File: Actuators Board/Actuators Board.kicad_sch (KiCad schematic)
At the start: 68 parts, among them IC1 BD62120AEFJ-E2, J1 Conn_01x05_Male, J10 Conn_01x02_Male, J2 Solenoid(Sol), J4 Conn_01x03_Male, J5 Conn_01x06_Male, J9 Conn_01x02_Male, Q1 MMDT2222A, Q2 SI2366DS, U1 ESP32-PICO-D4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

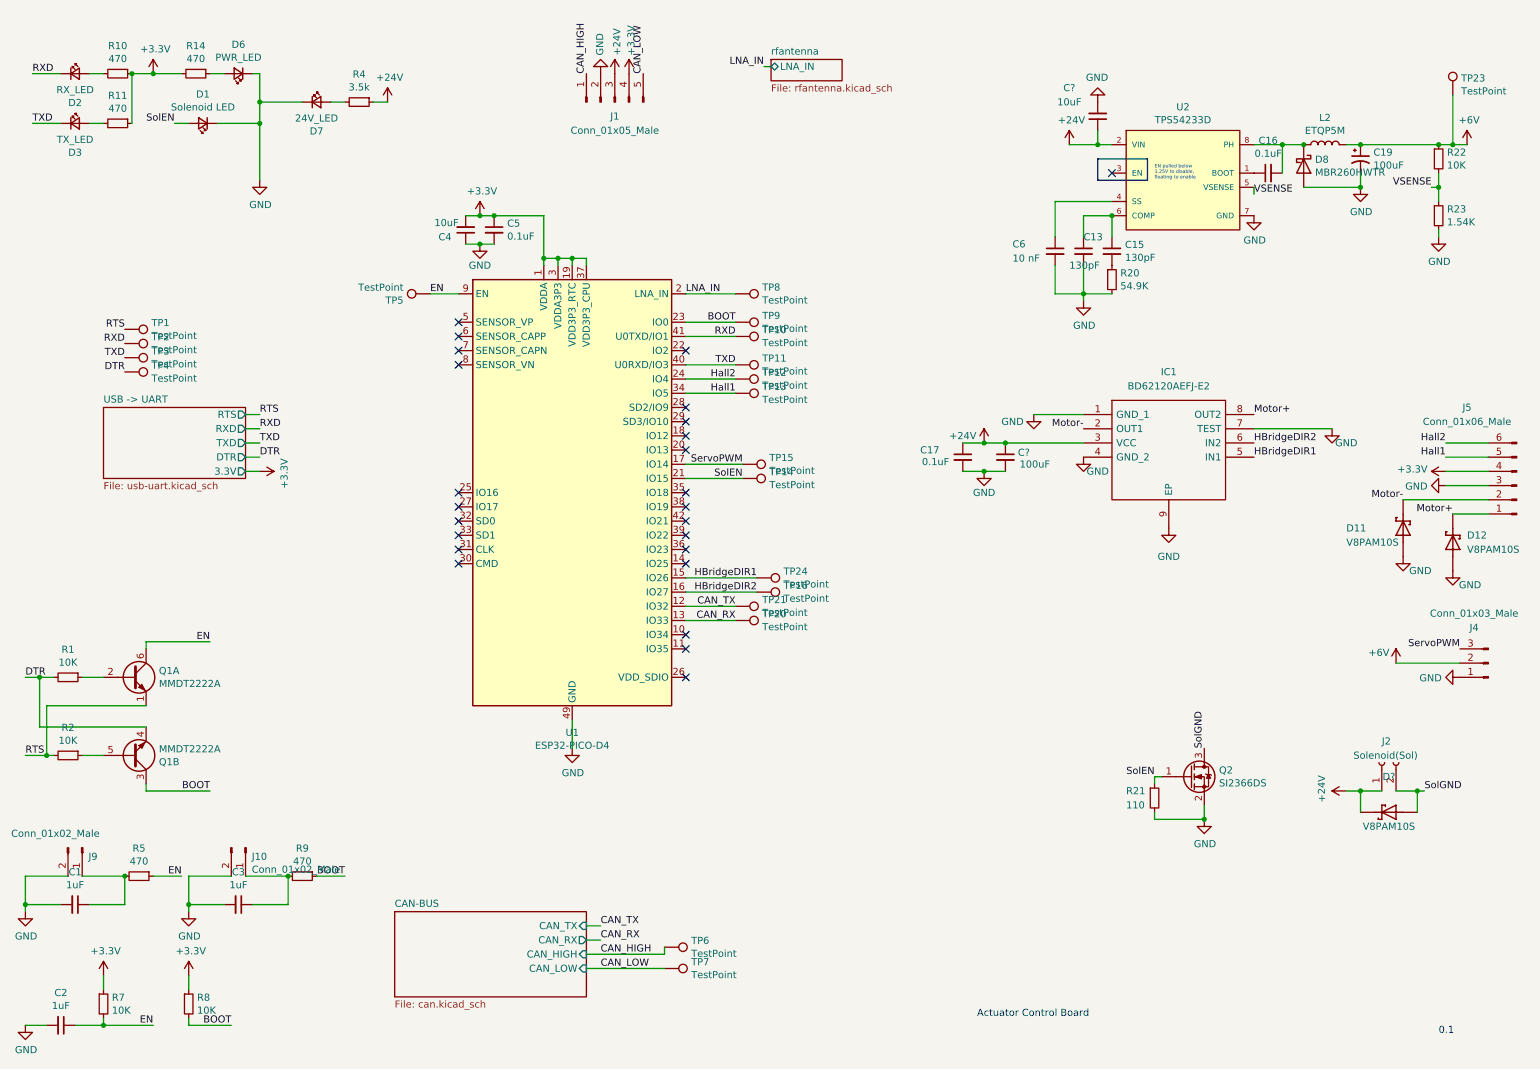
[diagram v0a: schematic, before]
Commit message: Added LDO for 5 -> 3.3V
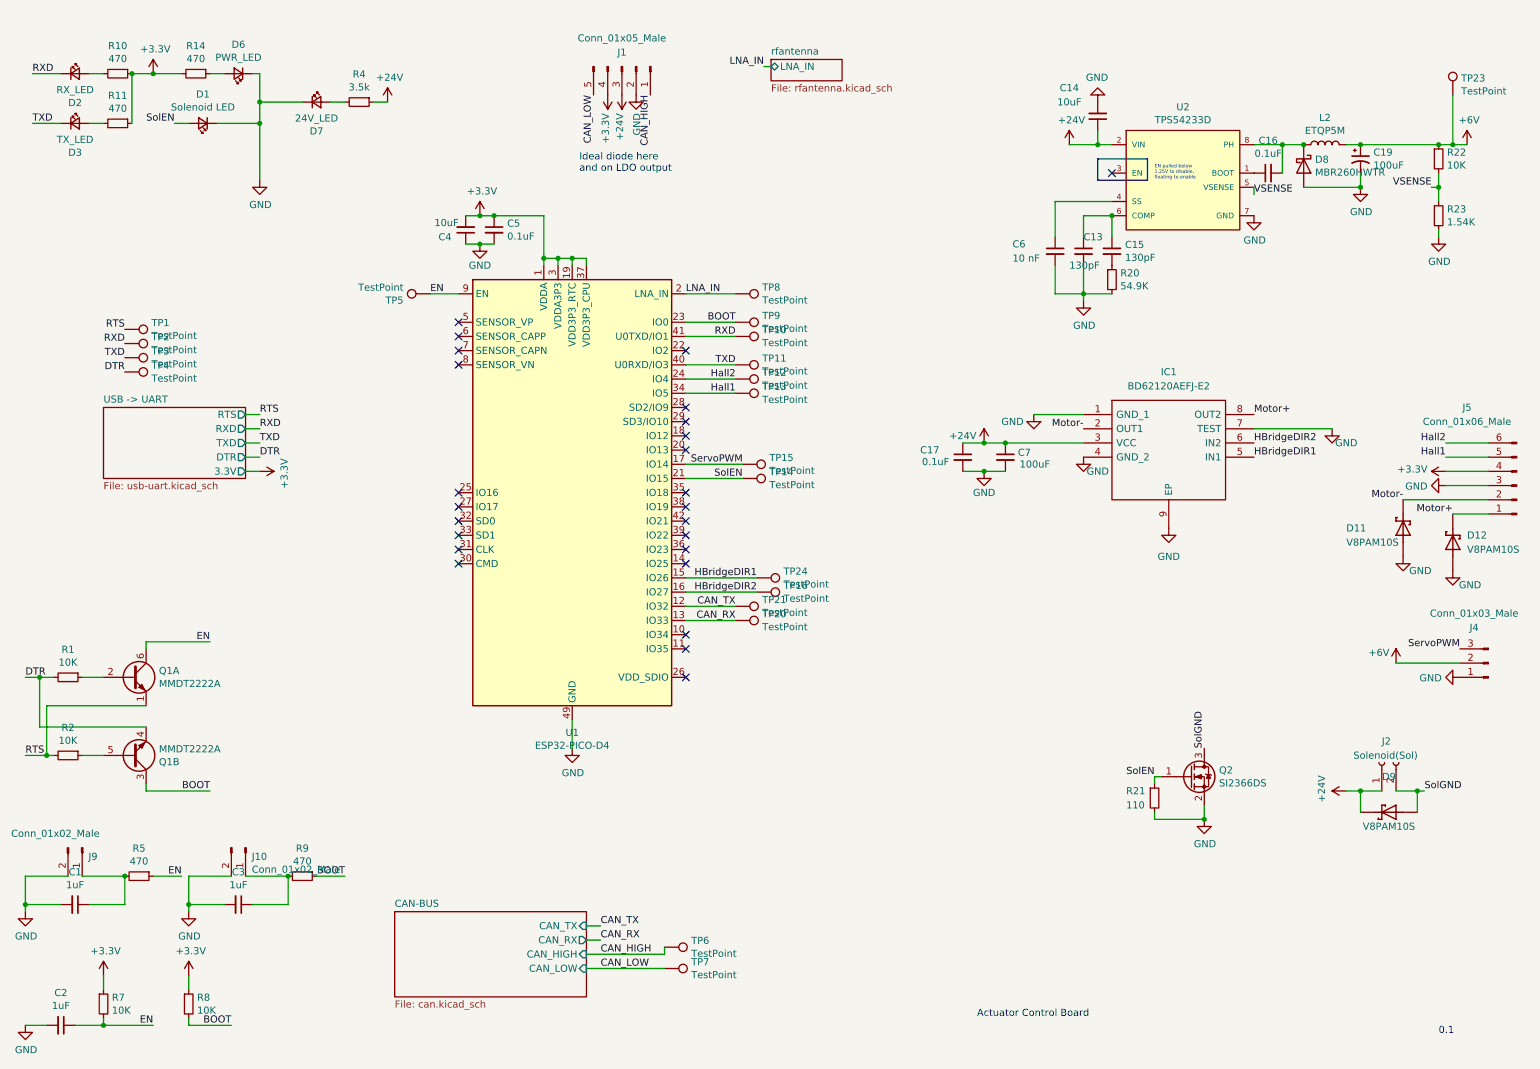
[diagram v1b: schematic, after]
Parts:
- gave numbers to parts that had none: 3
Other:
- note added: "Ideal diode here and on LDO output"
- moved on the sheet: J1

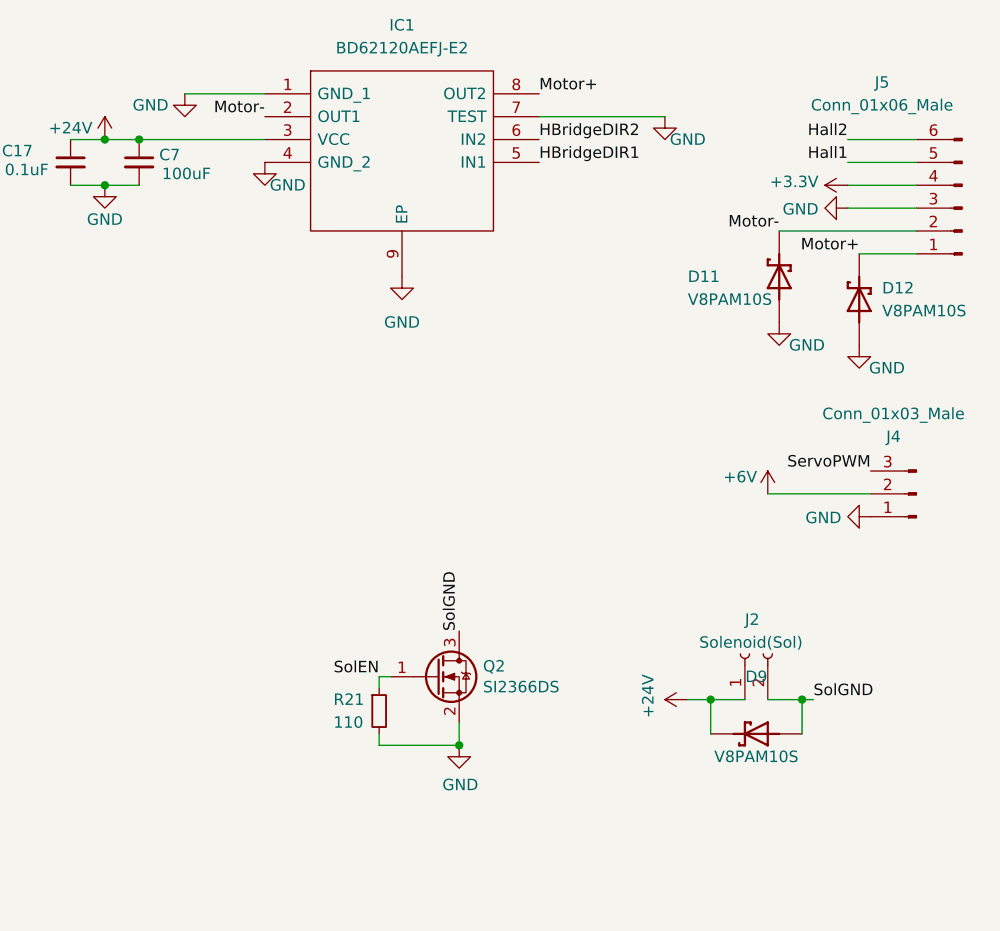
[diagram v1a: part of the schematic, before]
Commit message: Footprint assignments for capacitors+changed resistors on solenoid FET
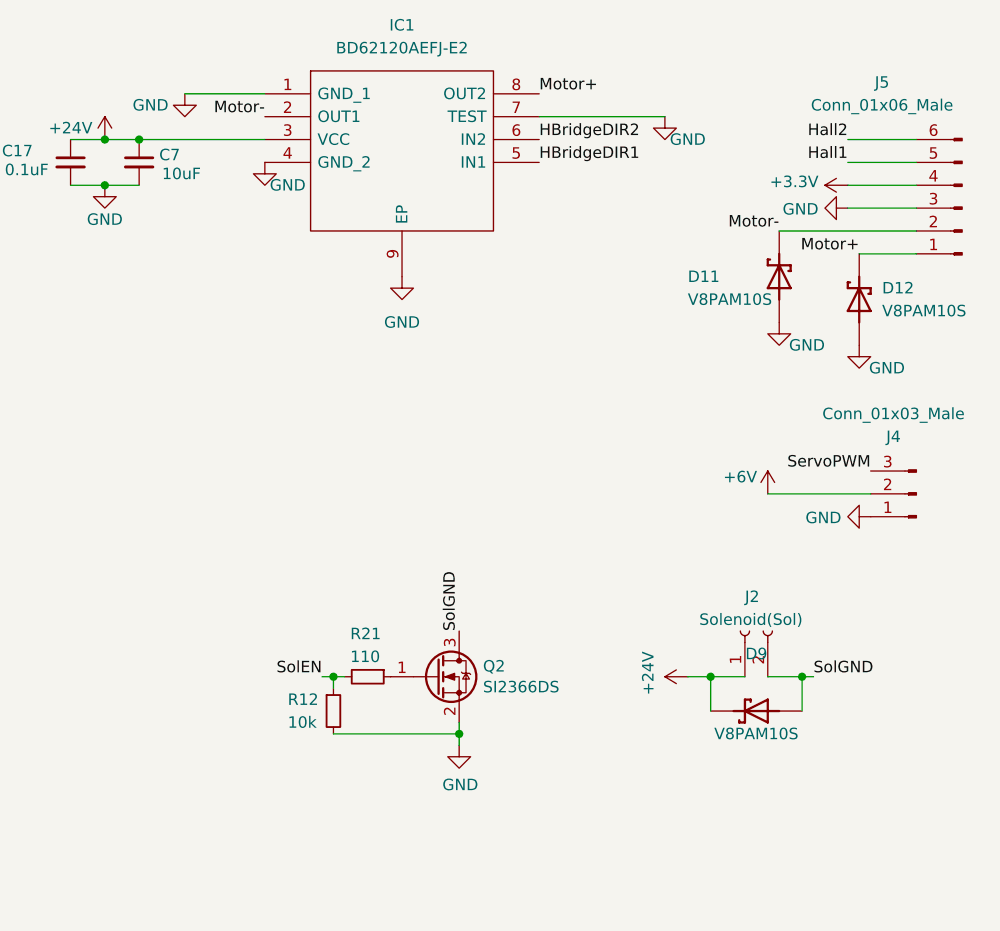
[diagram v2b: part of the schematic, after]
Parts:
- added R12: 10k, Resistor_SMD:R_0603_1608Metric, symbol Device:R_Small
- C14: footprint Capacitor_SMD:C_0603_1608Metric -> Capacitor_SMD:C_1210_3225Metric
- C7: value 100uF -> 10uF; footprint Capacitor_SMD:C_0603_1608Metric -> Capacitor_SMD:C_1210_3225Metric
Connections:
- net GND: now also R12.2; no longer R21.2
- net SolEN: now also R21.2, R12.1; no longer Q2.1 (G), R21.1
- new net: Q2.1 (G), R21.1
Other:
- moved on the sheet: D9, J2, R21

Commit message: ideal diode added
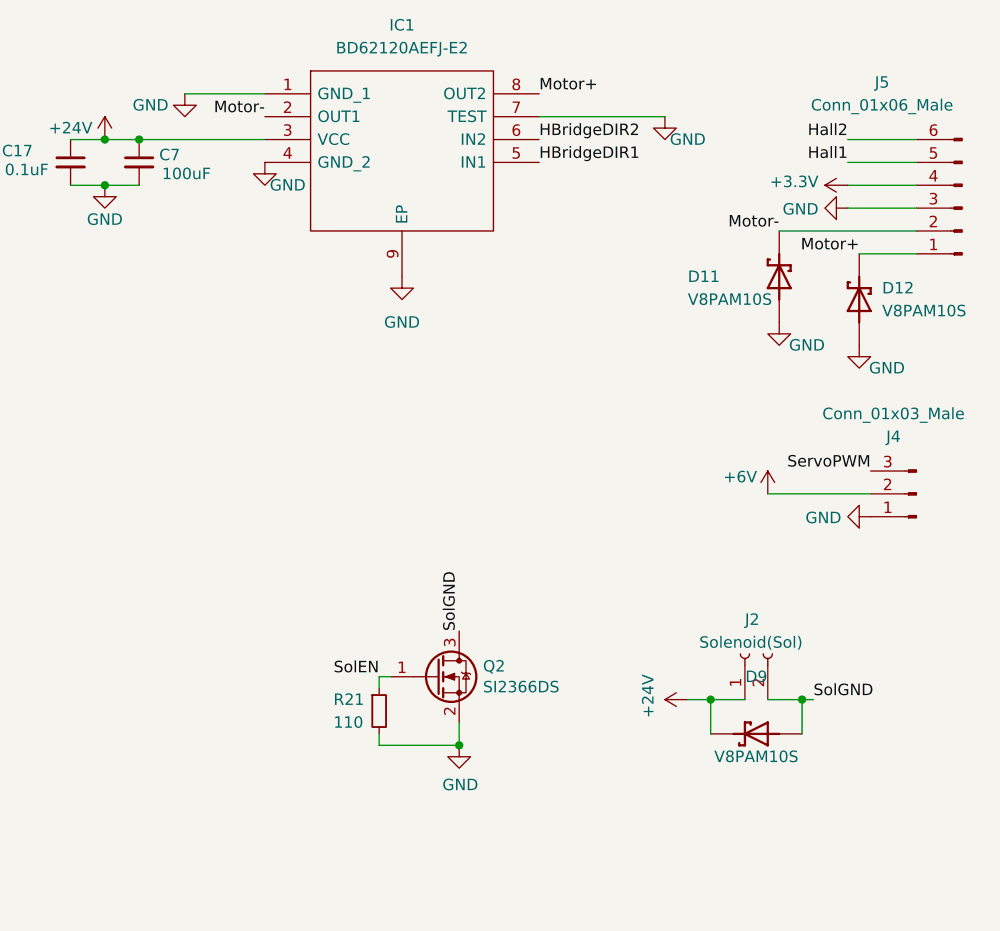
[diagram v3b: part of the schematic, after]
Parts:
- removed R12: 10k, Resistor_SMD:R_0603_1608Metric, symbol Device:R_Small
- C14: footprint Capacitor_SMD:C_1210_3225Metric -> Capacitor_SMD:C_0603_1608Metric
- C7: value 10uF -> 100uF; footprint Capacitor_SMD:C_1210_3225Metric -> Capacitor_SMD:C_0603_1608Metric
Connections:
- net GND: now also R21.2
- net SolEN: now also Q2.1 (G), R21.1; no longer R21.2
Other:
- moved on the sheet: D9, J2, R21

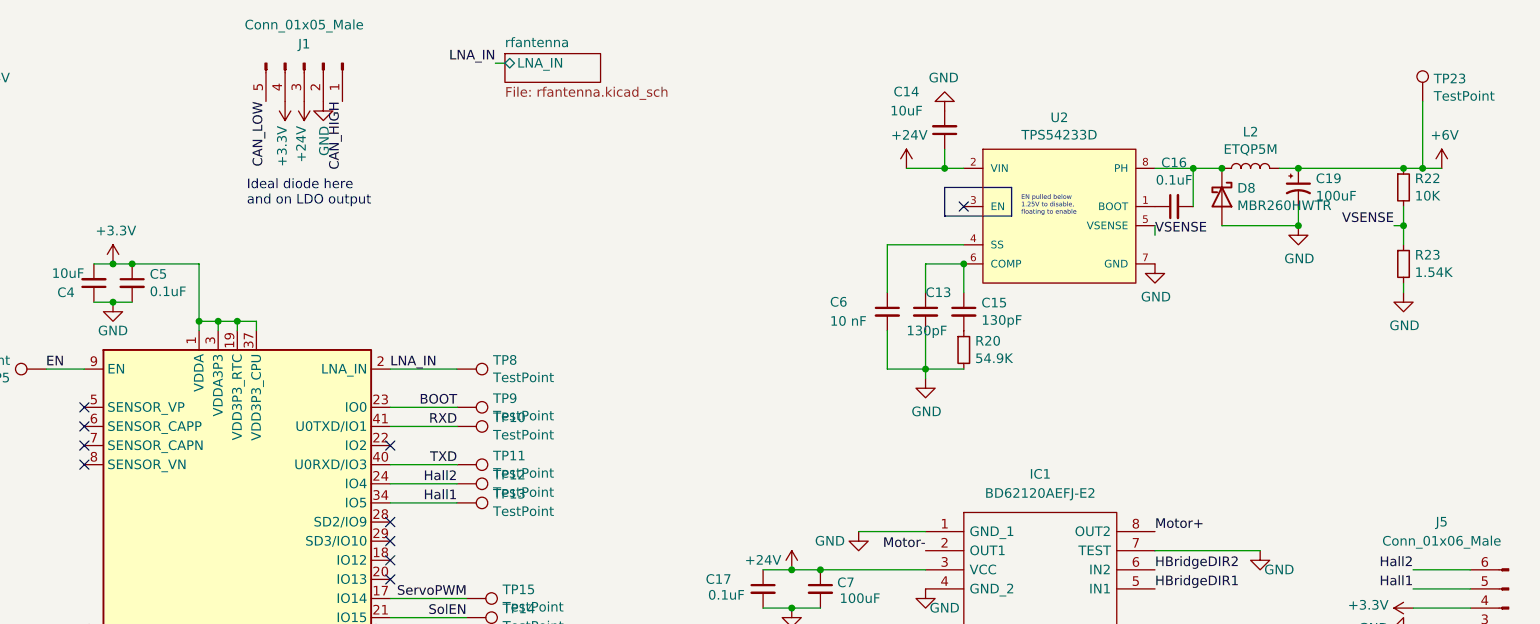
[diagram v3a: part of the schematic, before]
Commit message: added ideal diode for 3.3V con
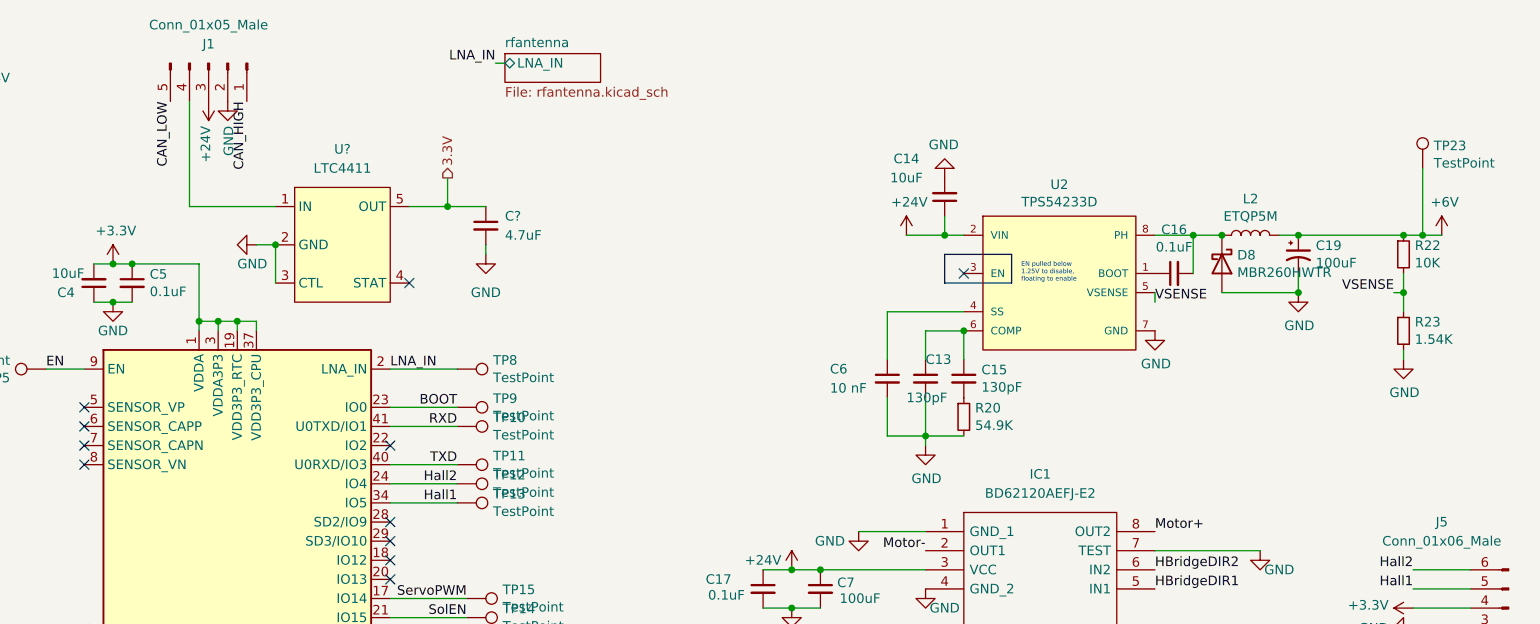
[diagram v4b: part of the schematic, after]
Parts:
- added C?: 4.7uF, symbol Device:C_Small
- added U?: LTC4411, symbol iclr:LTC4411
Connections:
- net +3V3: no longer J1.4 (Pin_4)
- net GND: now also C?.2, U?.2 (GND), U?.3 (CTL)
- new net: J1.4 (Pin_4), U?.1 (IN)
- new net 3.3V: C?.1, U?.5 (OUT)
- no-connect marks 25 -> 26
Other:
- note removed: "Ideal diode here and on LDO output"
- moved on the sheet: C13, C14, C15, C16, C19, C6, D8, J1, L2, R20, R22, R23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
